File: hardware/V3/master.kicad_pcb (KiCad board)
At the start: 4 copper layers, 40 x 40 mm, 127 parts, among them J1 USB-C, J2 DRILL, J3 DRILL, J4 DRILL, J5 DRILL, J6 STACK-UP-LOW, J7 STACK-DOWN, J8 STACK-UP-LOW, J9 STACK-DOWN, P1 Port A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

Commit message: fix descriptions
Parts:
- J6, J8: value STACK-UP-LOW -> STACK-UP-HIGH
- U1: value SAM??? -> SAM4S4CA
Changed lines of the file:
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@@
       (effects (font (size 0.3 0.3) (thickness 0.075)))
     )
-    (fp_text value STACK-UP-LOW (at -0.075 -0.325 90) (layer F.Fab)
+    (fp_text value STACK-UP-HIGH (at -0.075 -0.325 90) (layer F.Fab)
       (effects (font (size 0.3 0.3) (thickness 0.075)))
     )
@@
       (effects (font (size 0.3 0.3) (thickness 0.075)))
     )
-    (fp_text value STACK-UP-LOW (at -0.075 -0.325 90) (layer F.Fab)
+    (fp_text value STACK-UP-HIGH (at -0.075 -0.325 90) (layer F.Fab)
       (effects (font (size 0.3 0.3) (thickness 0.075)))
     )
@@
       (effects (font (size 0.29972 0.29972) (thickness 0.07493)))
     )
-    (fp_text value SAM??? (at 0 0 90) (layer F.Fab)
+    (fp_text value SAM4S4CA (at 0 0 90) (layer F.Fab)
       (effects (font (size 1.00076 1.00076) (thickness 0.12446)))
     )

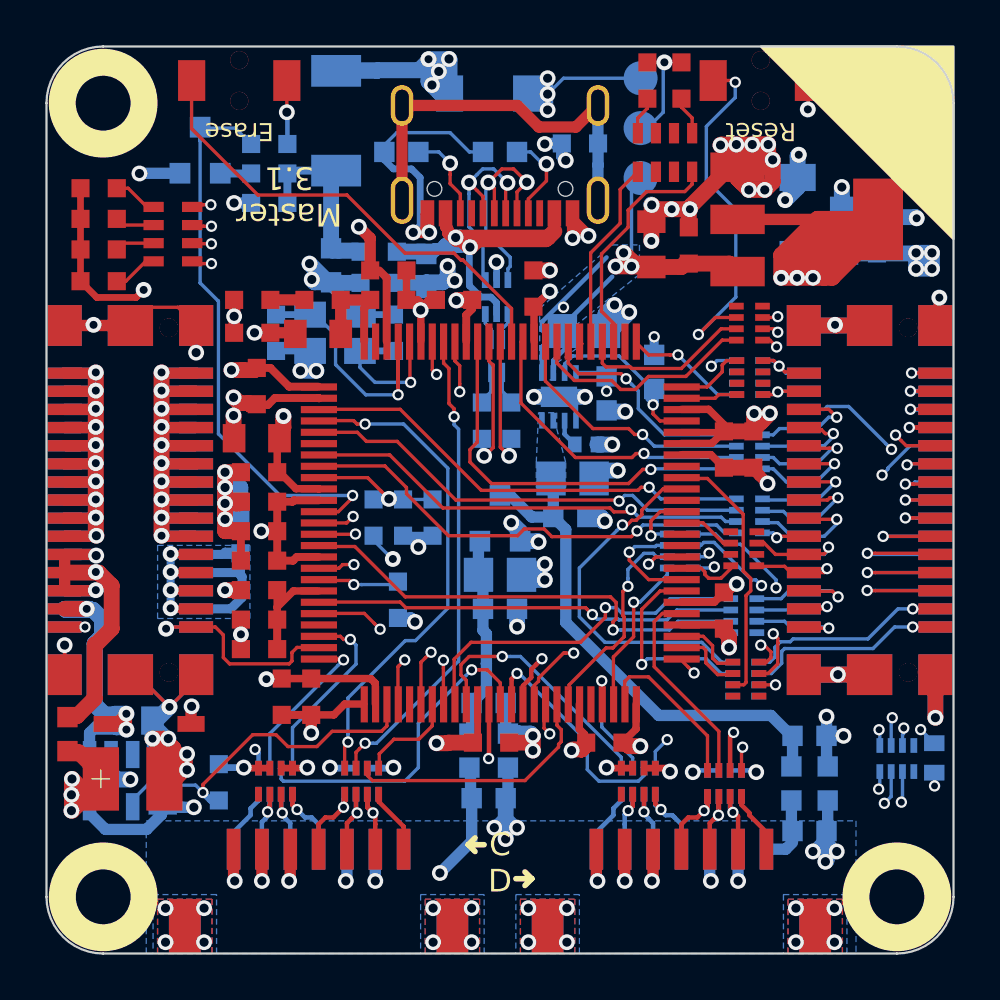
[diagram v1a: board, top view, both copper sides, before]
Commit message: add logos, add fiducials
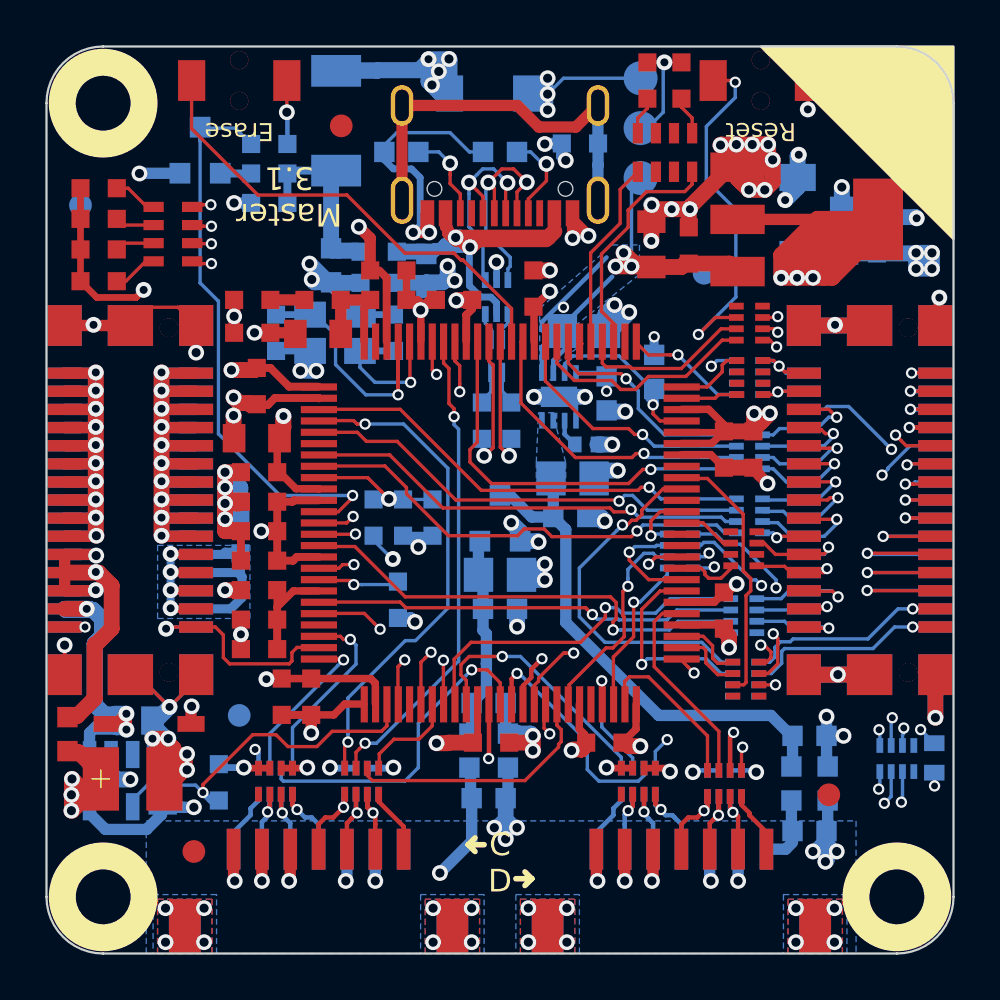
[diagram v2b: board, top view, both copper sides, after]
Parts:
- added Fiducial_Mark: VAL**, kicad-libraries:Fiducial_Mark, B.Cu at (154.0, 80.0)
- added Fiducial_Mark: VAL**, kicad-libraries:Fiducial_Mark, B.Cu at (126.5, 77.0)
- added Fiducial_Mark: VAL**, kicad-libraries:Fiducial_Mark, B.Cu at (133.5, 99.5)
- added Fiducial_Mark: VAL**, kicad-libraries:Fiducial_Mark, F.Cu at (159.5, 103.0)
- added Fiducial_Mark: VAL**, kicad-libraries:Fiducial_Mark, F.Cu at (131.5, 105.5)
- added Fiducial_Mark: VAL**, kicad-libraries:Fiducial_Mark, F.Cu at (138.0, 73.5)
- added G***: LOGO, kicad-libraries:Logo_31x31, B.Cu at (130.0, 78.0)
- added VAL: WEEE_7mm, kicad-libraries:WEEE_7mm, B.Cu at (138.0, 96.0)
- added VAL: CE_5mm, kicad-libraries:CE_5mm, B.Cu at (138.0, 86.5)

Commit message: version 3.2
add nrst improvement
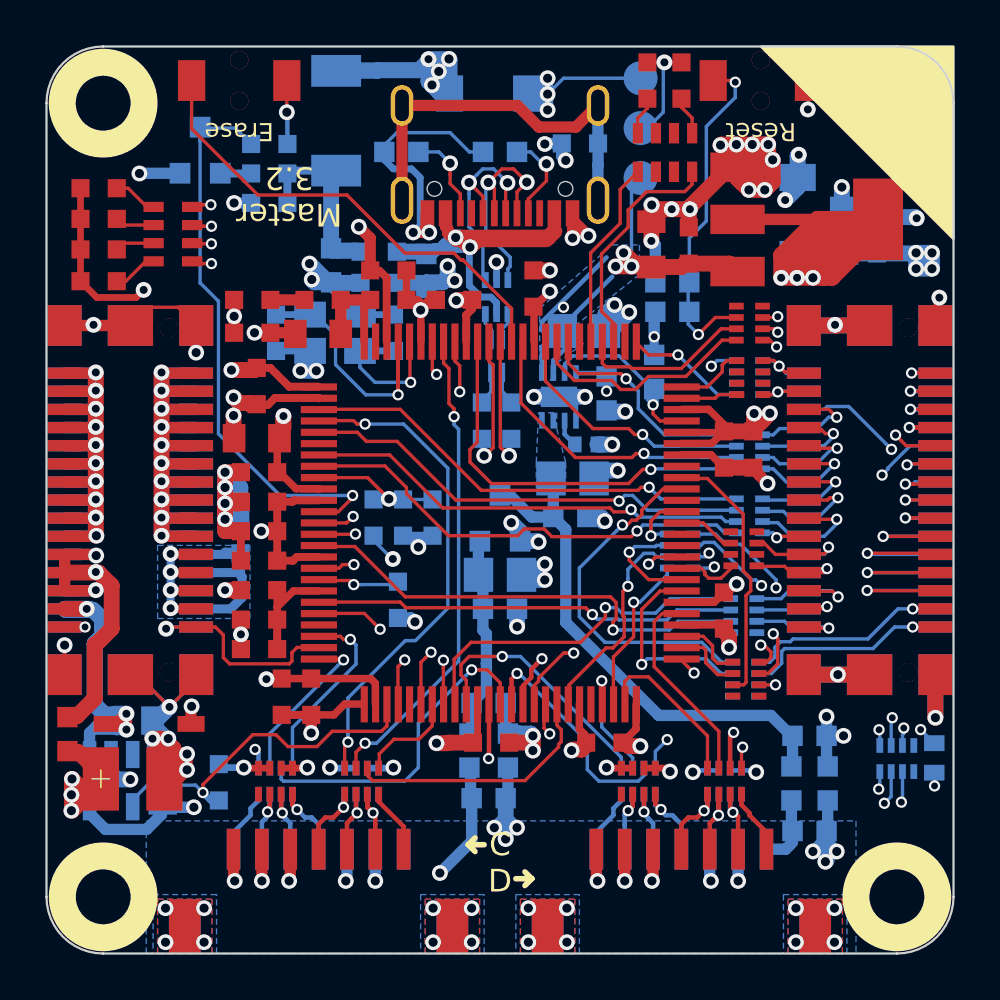
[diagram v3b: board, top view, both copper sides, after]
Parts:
- removed Fiducial_Mark (x6): VAL**, kicad-libraries:Fiducial_Mark
- removed G***: LOGO, kicad-libraries:Logo_31x31
- removed VAL: WEEE_7mm, kicad-libraries:WEEE_7mm
- removed VAL: CE_5mm, kicad-libraries:CE_5mm
- added C101: 4.7nF, kicad-libraries:C0603F, B.Cu at (152.6, 80.4)
- added R101: 100k, kicad-libraries:R0603F, B.Cu at (152.6, 81.7)
- J7: value STACK-DOWN -> STACK-HIGH
- J8: value STACK-UP-HIGH -> STACK-UP-LOW
- moved CP4 0.10 mm to (154.9, 102.4)
- moved RP9 0.10 mm to (154.9, 102.4)
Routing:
- net GND: track 215.6 -> 217.4 mm
- net 3V3: track 107.6 -> 108.8 mm
- net STACK-RESET: track 29.5 -> 28.8 mm
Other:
- board text added: "Master 3.2"
- board text removed: "Master 3.1"
